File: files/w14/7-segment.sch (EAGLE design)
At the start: 19 parts

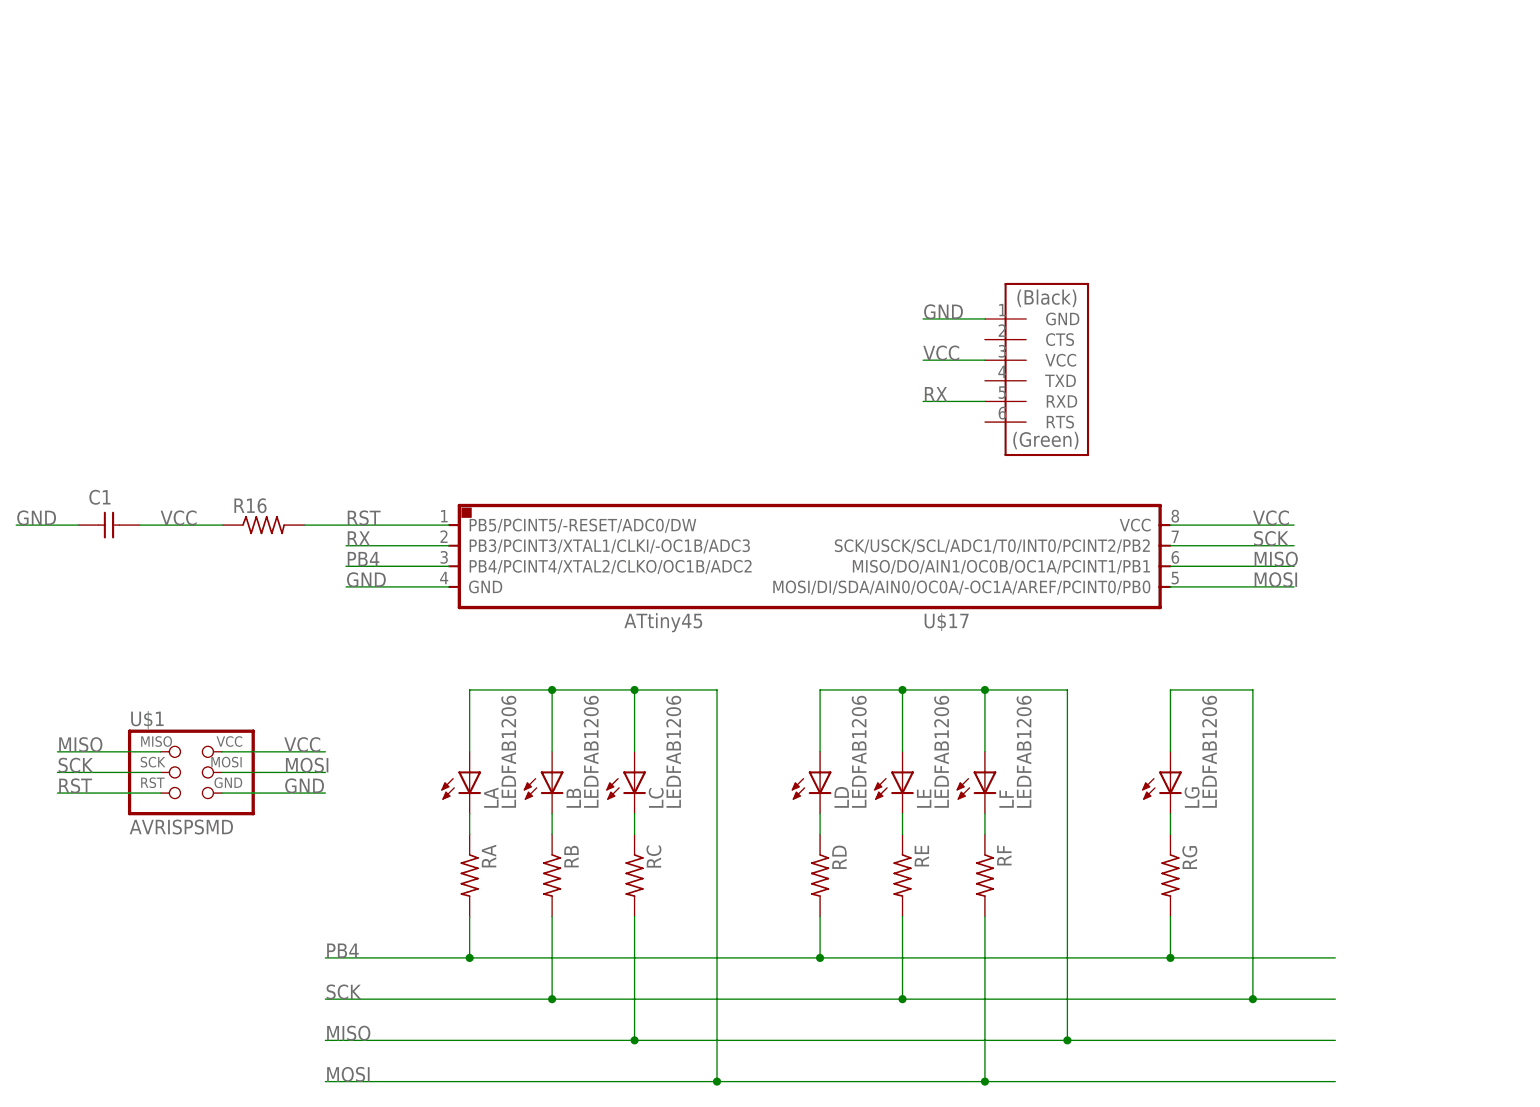
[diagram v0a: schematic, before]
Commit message: schematic without ISP header done
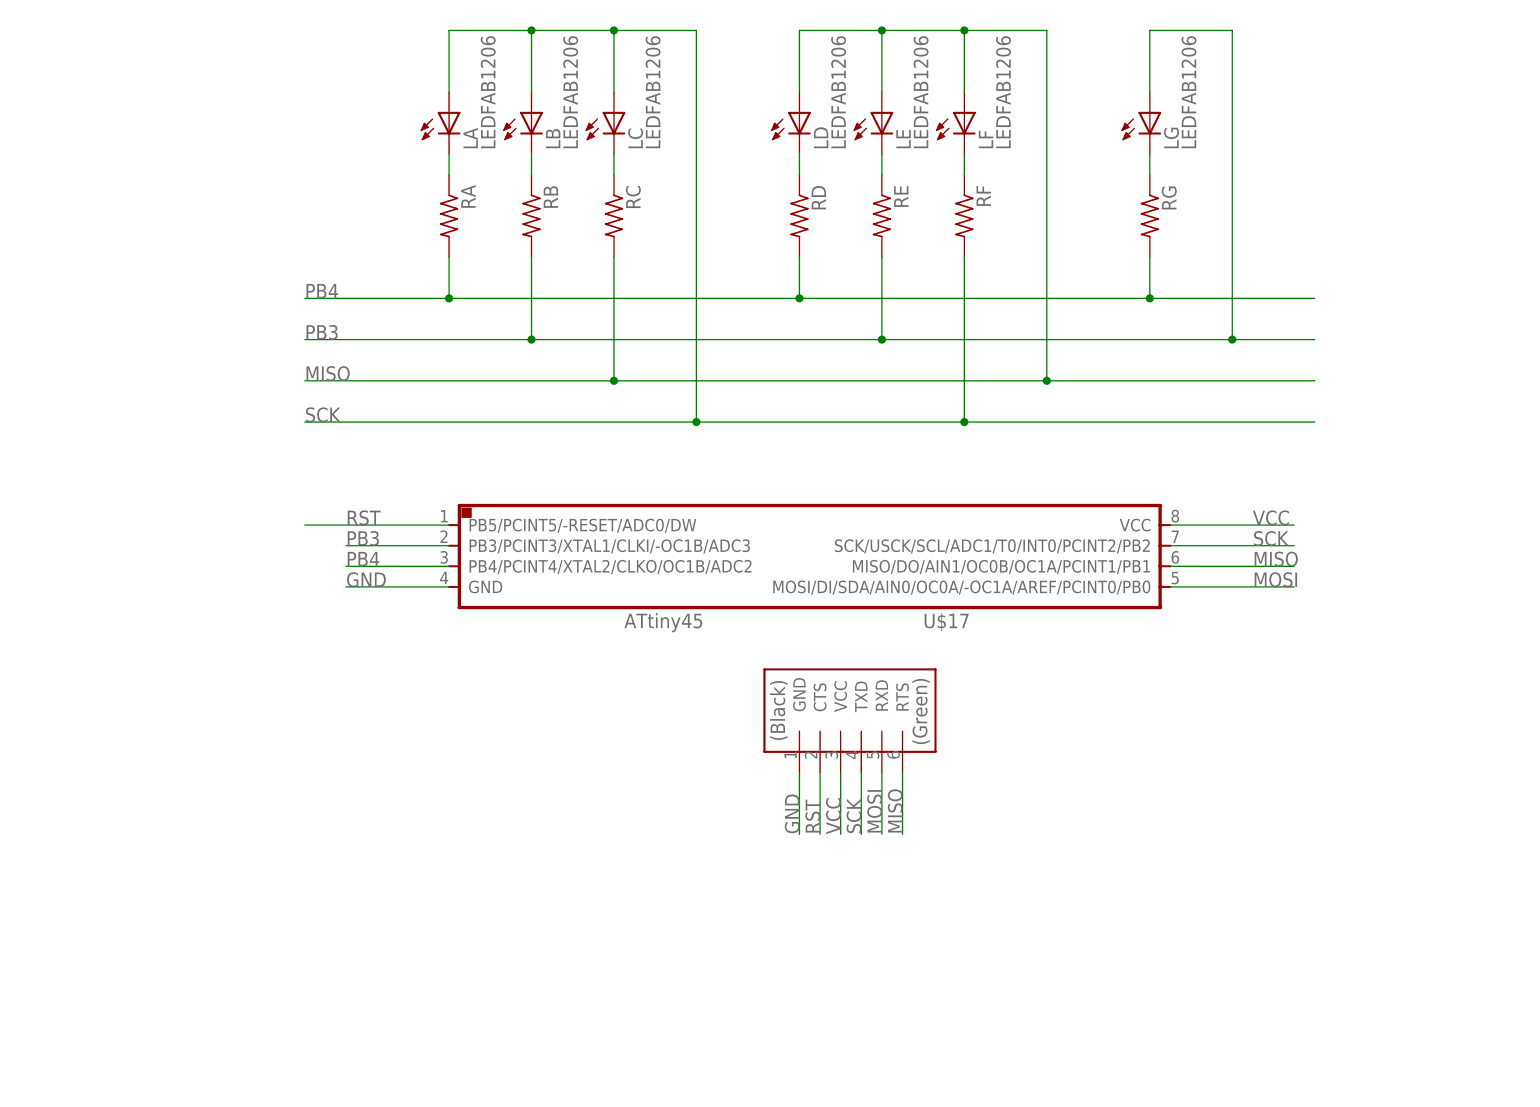
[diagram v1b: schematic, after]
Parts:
- removed C1: (no value), fab:CAP-UNPOLARIZEDFAB
- removed R16: (no value), fab:RES-US1206FAB
- removed U$1: AVRISPSMD, fab:AVRISPSMD
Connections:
- removed net RX: U$17.PB3/PCINT3/XTAL1/CLKI/-OC1B/ADC3, U$3.RXD
- new net PB3: LG.A, RB.2, RE.2, U$17.PB3/PCINT3/XTAL1/CLKI/-OC1B/ADC3
- net GND: no longer C1.1, U$1.GND
- net MISO: now also U$3.RTS; no longer U$1.MISO
- net MOSI: now also U$3.RXD; no longer LA.A, LB.A, LC.A, RF.2, U$1.MOSI
- net RST: now also U$3.CTS; no longer R16.2, U$1.RST
- net SCK: now also LA.A, LB.A, LC.A, RF.2, U$3.TXD; no longer LG.A, RB.2, RE.2, U$1.SCK
- net VCC: no longer C1.2, R16.1, U$1.VCC
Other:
- moved on the sheet: LA, LB, LC, LD, LE, LF, LG, RA, RB, RC, RD, RE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

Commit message: board programmed
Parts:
- added R1: 0, fab:RES-US1206FAB
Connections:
- net MISO: now also U$3.RXD; no longer LD.A, LE.A, LF.A, RC.2, U$3.RTS
- net MOSI: now also LD.A, LE.A, LF.A, RC.2, U$3.RTS; no longer U$3.RXD
- net PB3: now also R1.1, R1.2
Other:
- moved on the sheet: U$17
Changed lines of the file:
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@@
 <part name="LG" library="fab" deviceset="LED" device="FAB1206"/>
 <part name="U$3" library="fab" deviceset="FTDI-SMD-HEADER" device=""/>
+<part name="R1" library="fab" deviceset="RES-US" device="1206FAB" value="0"/>
 </parts>
 <sheets>
@@
 </plain>
 <instances>
-<instance part="U$17" gate="G$1" x="81.28" y="81.28"/>
+<instance part="U$17" gate="G$1" x="68.58" y="86.36" rot="R180"/>
 <instance part="RA" gate="G$1" x="27.94" y="124.46" rot="R270"/>
 <instance part="LA" gate="G$1" x="27.94" y="134.62"/>
@@
 <instance part="RG" gate="G$1" x="114.3" y="124.46" rot="R270"/>
 <instance part="LG" gate="G$1" x="114.3" y="134.62"/>
-<instance part="U$3" gate="G$1" x="83.82" y="55.88" rot="R90"/>
+<instance part="U$3" gate="G$1" x="71.12" y="58.42" rot="R270"/>
+<instance part="R1" gate="G$1" x="147.32" y="83.82"/>
 </instances>
 <busses>
@@
 <segment>
 <pinref part="U$17" gate="G$1" pin="VCC"/>
-<wire x1="116.84" y1="86.36" x2="132.08" y2="86.36" width="0.1524" layer="91"/>
-<label x="127" y="86.36" size="1.778" layer="95"/>
+<wire x1="33.02" y1="81.28" x2="17.78" y2="81.28" width="0.1524" layer="91"/>
+<label x="22.86" y="81.28" size="1.778" layer="95" rot="R180"/>
 </segment>
 <segment>
 <pinref part="U$3" gate="G$1" pin="VCC"/>
-<wire x1="76.2" y1="55.88" x2="76.2" y2="48.26" width="0.1524" layer="91"/>
-<label x="76.2" y="48.26" size="1.778" layer="95" rot="R90"/>
+<wire x1="78.74" y1="58.42" x2="78.74" y2="66.04" width="0.1524" layer="91"/>
+<label x="78.74" y="66.04" size="1.778" layer="95" rot="R270"/>
 </segment>
 </net>
@@
 <segment>
 <pinref part="U$17" gate="G$1" pin="GND"/>
-<wire x1="27.94" y1="78.74" x2="15.24" y2="78.74" width="0.1524" layer="91"/>
-<label x="15.24" y="78.74" size="1.778" layer="95"/>
+<wire x1="121.92" y1="88.9" x2="134.62" y2="88.9" width="0.1524" layer="91"/>
+<label x="134.62" y="88.9" size="1.778" layer="95" rot="R180"/>
 </segment>
 <segment>
 <pinref part="U$3" gate="G$1" pin="GND"/>
-<wire x1="71.12" y1="55.88" x2="71.12" y2="48.26" width="0.1524" layer="91"/>
-<label x="71.12" y="48.26" size="1.778" layer="95" rot="R90"/>
+<wire x1="83.82" y1="58.42" x2="83.82" y2="66.04" width="0.1524" layer="91"/>
+<label x="83.82" y="66.04" size="1.778" layer="95" rot="R270"/>
 </segment>
 </net>
@@
 <segment>
 <pinref part="U$17" gate="G$1" pin="PB5/PCINT5/-RESET/ADC0/DW"/>
-<wire x1="27.94" y1="86.36" x2="10.16" y2="86.36" width="0.1524" layer="91"/>
-<label x="15.24" y="86.36" size="1.778" layer="95"/>
+<wire x1="121.92" y1="81.28" x2="134.62" y2="81.28" width="0.1524" layer="91"/>
+<label x="134.62" y="81.28" size="1.778" layer="95" rot="R180"/>
 </segment>
 <segment>
 <pinref part="U$3" gate="G$1" pin="CTS"/>
-<wire x1="73.66" y1="55.88" x2="73.66" y2="48.26" width="0.1524" layer="91"/>
-<label x="73.66" y="48.26" size="1.778" layer="95" rot="R90"/>
+<wire x1="81.28" y1="58.42" x2="81.28" y2="66.04" width="0.1524" layer="91"/>
+<label x="81.28" y="66.04" size="1.778" layer="95" rot="R270"/>
 </segment>
 </net>
@@
 <segment>
 <pinref part="U$17" gate="G$1" pin="MOSI/DI/SDA/AIN0/OC0A/-OC1A/AREF/PCINT0/PB0"/>
-<wire x1="116.84" y1="78.74" x2="132.08" y2="78.74" width="0.1524" layer="91"/>
-<label x="127" y="78.74" size="1.778" layer="95"/>
-</segment>
-<segment>
-<pinref part="U$3" gate="G$1" pin="RXD"/>
-<wire x1="81.28" y1="55.88" x2="81.28" y2="48.26" width="0.1524" layer="91"/>
-<label x="81.28" y="48.26" size="1.778" layer="95" rot="R90"/>
-</segment>
-</net>
-<net name="MISO" class="0">
-<segment>
-<pinref part="U$17" gate="G$1" pin="MISO/DO/AIN1/OC0B/OC1A/PCINT1/PB1"/>
-<wire x1="116.84" y1="81.28" x2="132.08" y2="81.28" width="0.1524" layer="91"/>
-<label x="127" y="81.28" size="1.778" layer="95"/>
+<wire x1="33.02" y1="88.9" x2="17.78" y2="88.9" width="0.1524" layer="91"/>
+<label x="22.86" y="88.9" size="1.778" layer="95" rot="R180"/>
+</segment>
+<segment>
+<pinref part="U$3" gate="G$1" pin="RTS"/>
+<wire x1="71.12" y1="58.42" x2="71.12" y2="66.04" width="0.1524" layer="91"/>
+<label x="71.12" y="66.04" size="1.778" layer="95" rot="R270"/>
 </segment>
 <segment>
@@
 <label x="10.16" y="104.14" size="1.778" layer="95"/>
 </segment>
-<segment>
-<pinref part="U$3" gate="G$1" pin="RTS"/>
-<wire x1="83.82" y1="55.88" x2="83.82" y2="48.26" width="0.1524" layer="91"/>
-<label x="83.82" y="48.26" size="1.778" layer="95" rot="R90"/>
+</net>
+<net name="MISO" class="0">
+<segment>
+<pinref part="U$17" gate="G$1" pin="MISO/DO/AIN1/OC0B/OC1A/PCINT1/PB1"/>
+<wire x1="33.02" y1="86.36" x2="17.78" y2="86.36" width="0.1524" layer="91"/>
+<label x="22.86" y="86.36" size="1.778" layer="95" rot="R180"/>
+</segment>
+<segment>
+<pinref part="U$3" gate="G$1" pin="RXD"/>
+<wire x1="73.66" y1="58.42" x2="73.66" y2="66.04" width="0.1524" layer="91"/>
+<label x="73.66" y="66.04" size="1.778" layer="95" rot="R270"/>
 </segment>
 </net>
@@
 <segment>
 <pinref part="U$17" gate="G$1" pin="SCK/USCK/SCL/ADC1/T0/INT0/PCINT2/PB2"/>
-<wire x1="116.84" y1="83.82" x2="132.08" y2="83.82" width="0.1524" layer="91"/>
-<label x="127" y="83.82" size="1.778" layer="95"/>
+<wire x1="33.02" y1="83.82" x2="17.78" y2="83.82" width="0.1524" layer="91"/>
+<label x="22.86" y="83.82" size="1.778" layer="95" rot="R180"/>
 </segment>
 <segment>
@@
 <segment>
 <pinref part="U$3" gate="G$1" pin="TXD"/>
-<wire x1="78.74" y1="55.88" x2="78.74" y2="48.26" width="0.1524" layer="91"/>
-<label x="78.74" y="48.26" size="1.778" layer="95" rot="R90"/>
+<wire x1="76.2" y1="58.42" x2="76.2" y2="66.04" width="0.1524" layer="91"/>
+<label x="76.2" y="66.04" size="1.778" layer="95" rot="R270"/>
 </segment>
 </net>
@@
 <segment>
 <pinref part="U$17" gate="G$1" pin="PB4/PCINT4/XTAL2/CLKO/OC1B/ADC2"/>
-<wire x1="27.94" y1="81.28" x2="15.24" y2="81.28" width="0.1524" layer="91"/>
-<label x="15.24" y="81.28" size="1.778" layer="95"/>
+<wire x1="121.92" y1="86.36" x2="134.62" y2="86.36" width="0.1524" layer="91"/>
+<label x="134.62" y="86.36" size="1.778" layer="95" rot="R180"/>
 </segment>
 </net>
@@
 <segment>
 <pinref part="U$17" gate="G$1" pin="PB3/PCINT3/XTAL1/CLKI/-OC1B/ADC3"/>
-<wire x1="27.94" y1="83.82" x2="15.24" y2="83.82" width="0.1524" layer="91"/>
-<label x="15.24" y="83.82" size="1.778" layer="95"/>
+<wire x1="121.92" y1="83.82" x2="142.24" y2="83.82" width="0.1524" layer="91"/>
+<label x="134.62" y="83.82" size="1.778" layer="95" rot="R180"/>
+<pinref part="R1" gate="G$1" pin="1"/>
 </segment>
 <segment>
@@
 <label x="10.16" y="109.22" size="1.778" layer="95"/>
 </segment>
-</net>
+<segment>
+<pinref part="R1" gate="G$1" pin="2"/>
+<wire x1="152.4" y1="83.82" x2="160.02" y2="83.82" width="0.1524" layer="91"/>
+<label x="154.94" y="83.82" size="1.778" layer="95"/>
+</segment>
+</net>
